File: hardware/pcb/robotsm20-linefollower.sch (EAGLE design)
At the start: 120 parts, among them IC1 BNO055, IC2 TPS43061RTER, Q1 CSD15571Q2, Q2 CSD15571Q2, Q3 CSD15571Q2, Q4 CSD15571Q2, Q5 BSS138LT3G, Q6 BSS138LT3G, Q7 BSS138LT3G, U1 STM32F405RG

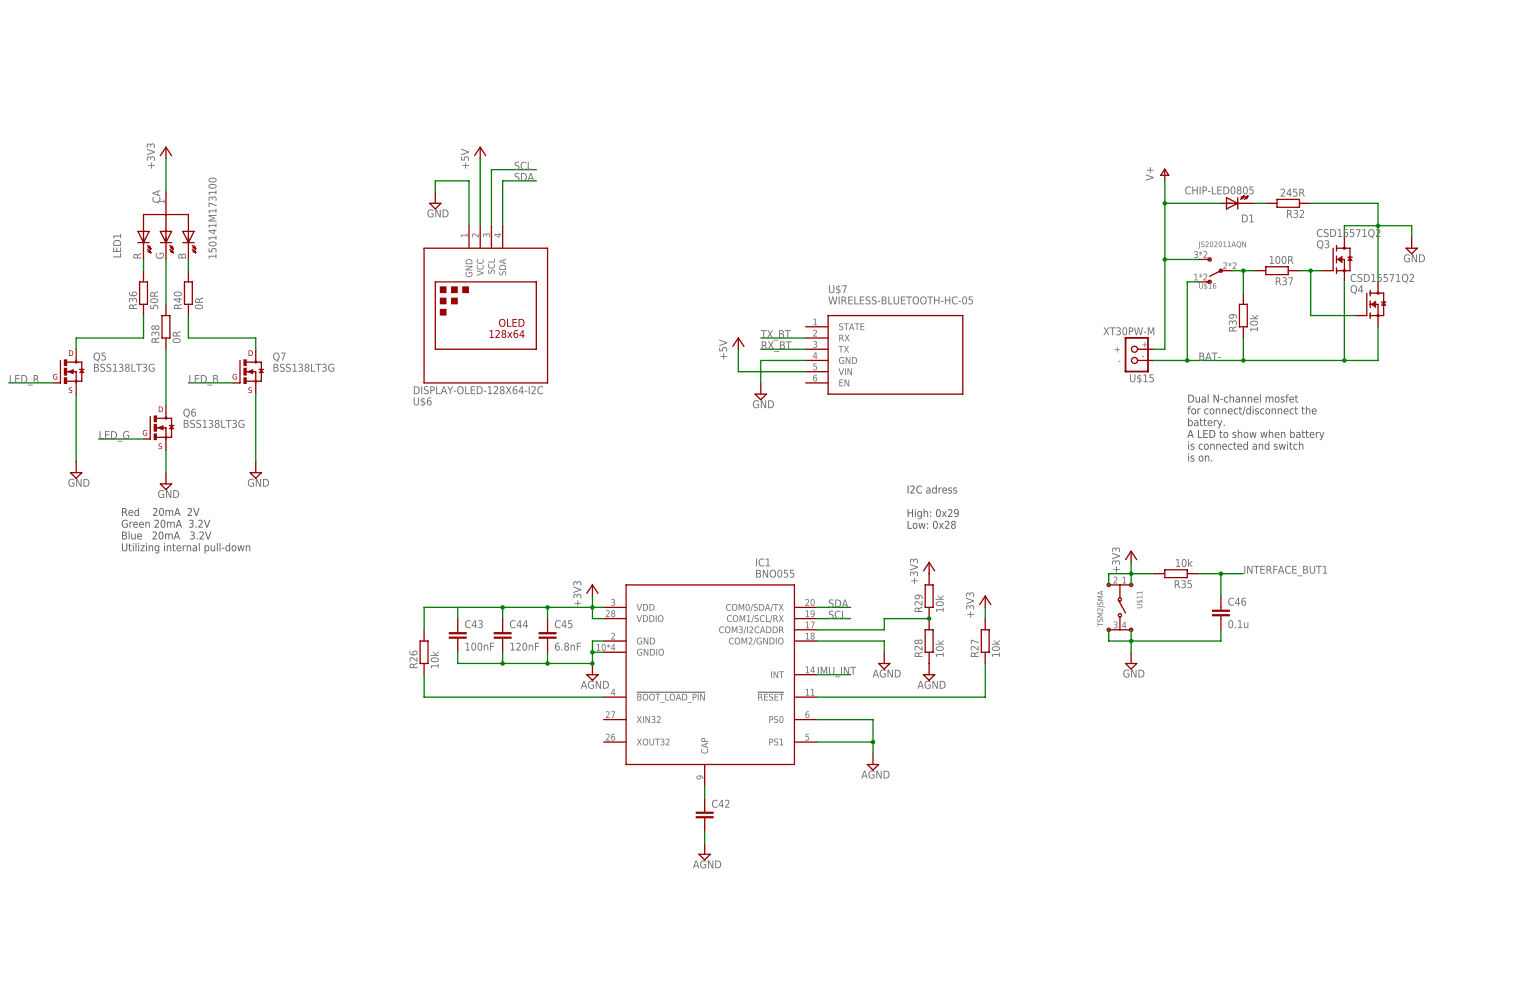
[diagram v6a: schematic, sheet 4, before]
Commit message: Added more connectors to motors and sensor
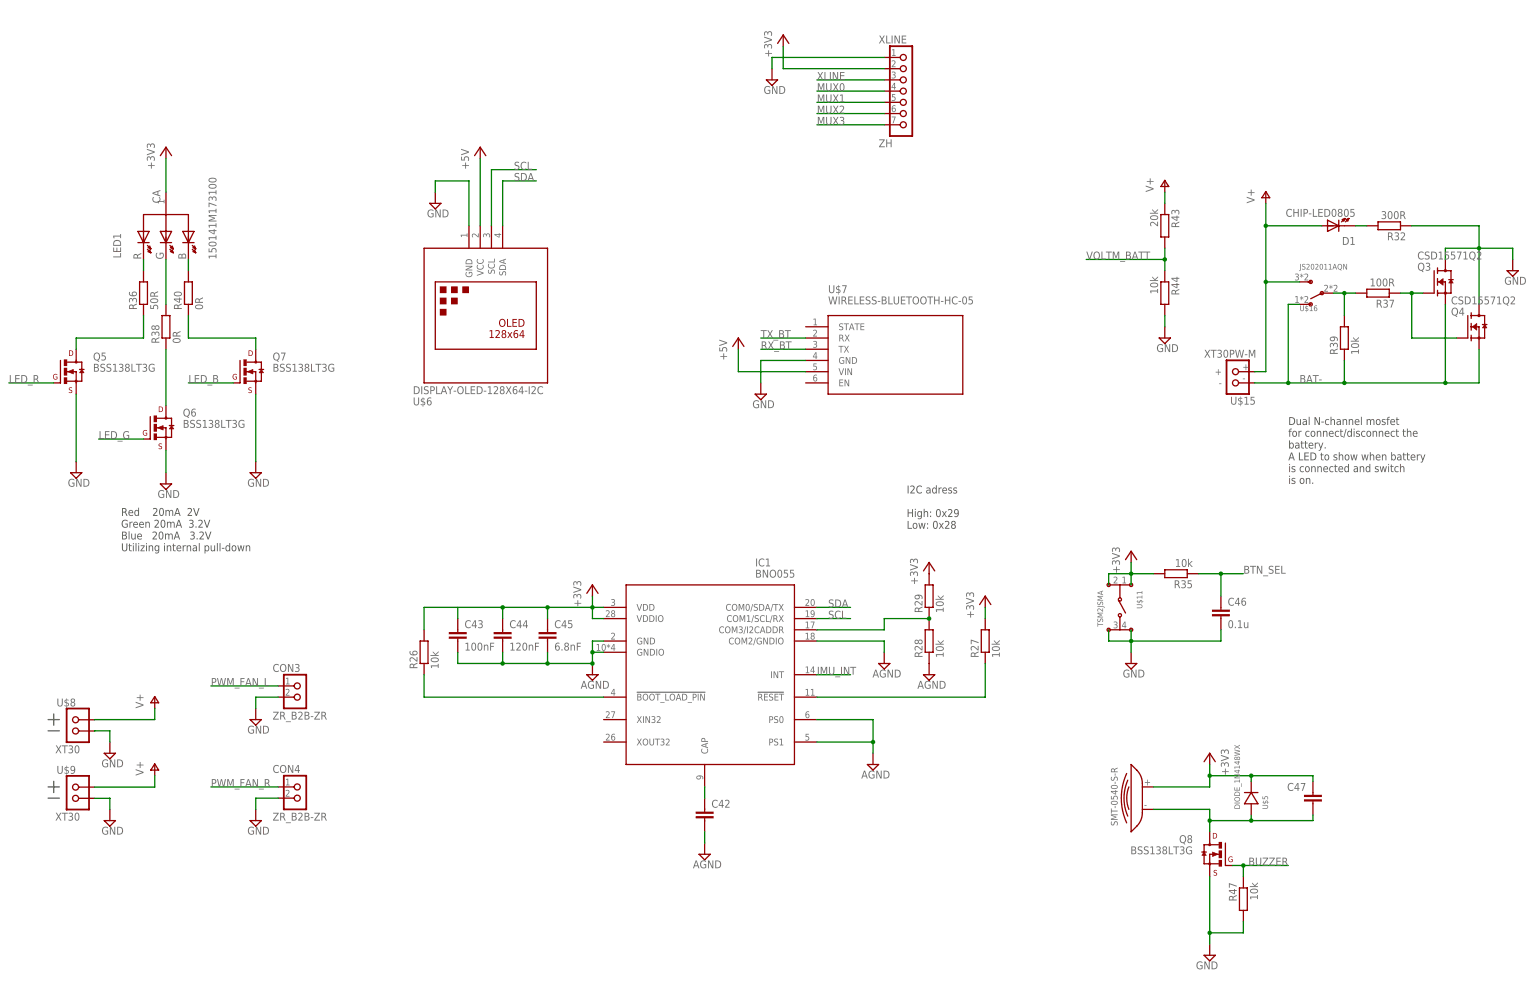
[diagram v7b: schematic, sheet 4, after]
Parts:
- added C47: (no value), rcl:C-EUC0805
- added CON3, CON4: ZR_B2B-ZR, CASE-JST:ZR_B2B-ZR
- added Q8: BSS138LT3G, CASE-Transistors:BSS138LT3G
- added R43: 20k, rcl:R-EU_R0603
- added R44, R45, R47: 10k, rcl:R-EU_R0603
- added R46: 62k, rcl:R-EU_R0603
- added U$1: SMT-0540-S-R, Isaks Bibliotek:SMT-0540-S-R
- added U$5: DIODE_1N4148WX, Isaks Bibliotek:DIODE_1N4148WX
- added U$8, U$9: XT30, CASE_DC-Connector:XT30
- added XLINE: ZH, CASE-JST:ZR_B7B-ZR
- R32: value 245R -> 300R
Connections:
- net N$66 renamed SDIO_CK
- net N$80 renamed SDIO_D0
- net VOLTM_CELL1 renamed N$25
- removed net 3.3V: BOOT.1, BOOT.2, C31.1, C32.1, C33.1, C34.1, C35.1, C37.1, C39.1, R30.1, R31.1, U1.VBAT, U1.VDDA, U1.VDD_1, U1.VDD_2, U1.VDD_3, U1.VDD_4
- removed net 3.3V1: R41.1, R42.1
- removed net CURA: C1.1, R3.2
- removed net CURB: C2.1, R4.2
- removed net GND1: PS2.GND
- removed net INTERFACE_BUT1: C46.1, R35.1
- removed net N$10: PS2.PAD, R8.1
- removed net N$25 (its old number): U1.PC0
- removed net N$35: U1.PC3
- removed net N$82: U1.PC6
- removed net N$83: U1.PC7
- removed net V+1: C14.1, PS2.EN, PS2.VIN
- new net MOTOR_L_CUR: C1.1, R3.2, U1.PC0
- new net MOTOR_R_CUR: C2.1, R4.2, U1.PC1
- new net PWM_FAN_L: CON3.1, U1.PC6
- new net PWM_FAN_R: CON4.1, U1.PC7
- new net SDIO_CMD: U1.PD2
- net +12V: now also R46.2
- net +3V3: now also BOOT.1, BOOT.2, C31.1, C32.1, C33.1, C34.1, C35.1, C37.1, C39.1, C47.1, R30.1, R31.1, R41.1, R42.1, U$1.+, U$5.-_CATHODE, U1.VBAT, U1.VDDA, U1.VDD_1, U1.VDD_2, U1.VDD_3, U1.VDD_4, XLINE.2
- net BTN_SEL: now also C46.1, R35.1, U1.PC3; no longer U1.PD2
- net BUZZER: now also Q8.G, R47.1
- net GND: now also CON3.2, CON4.2, PS2.GND, PS2.PAD, Q8.S, R44.2, R45.1, R47.2, R8.1, U$8.NEG-, U$9.NEG-, XLINE.1
- net MUX0: now also XLINE.4
- net MUX1: now also XLINE.5
- net MUX2: now also XLINE.6
- net MUX3: now also XLINE.7
- net N$33: now also C47.2, Q8.D, U$1.-, U$5.+_ANODE; no longer U1.PC1
- net V+: now also C14.1, PS2.EN, PS2.VIN, R43.1, U$8.POS+, U$9.POS+
- net VOLTM_BATT: now also R43.2, R44.1, R45.2, R46.1
- net XLINE: now also XLINE.3
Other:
- note added: "3V3 at 24V output"
- moved on the sheet: C1, C11, C12, C16, C17, C22, C23, C24, C25, C40, D1, Q3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

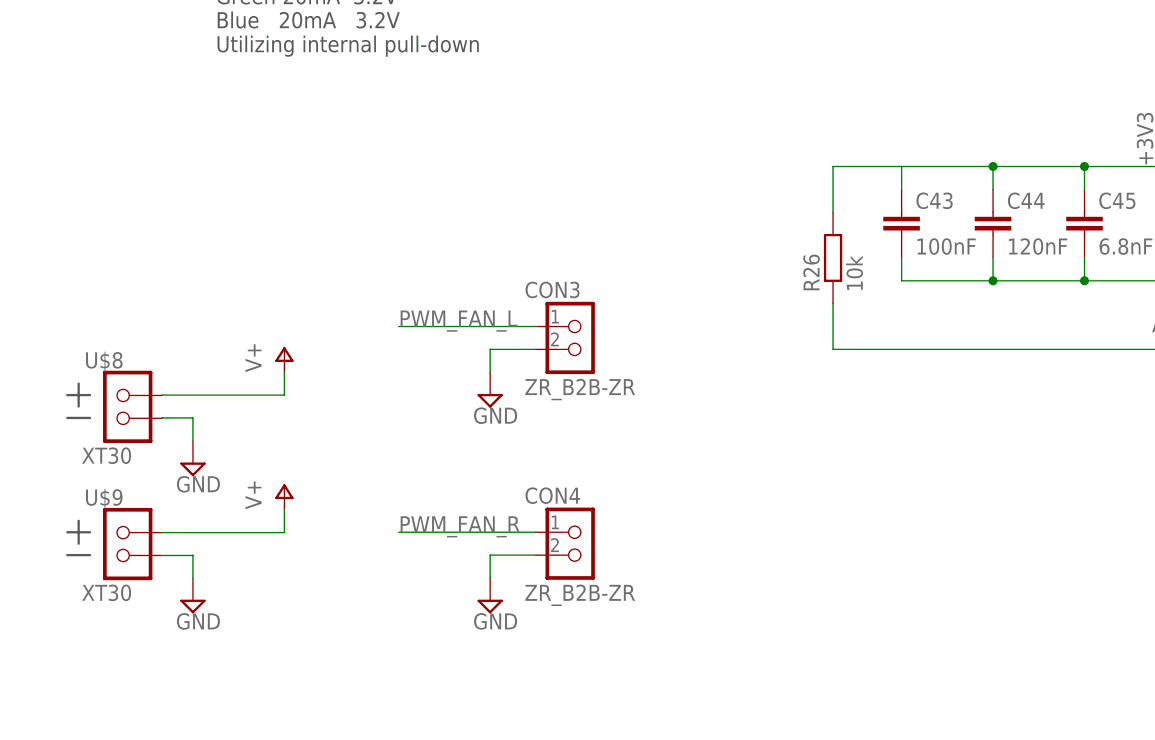
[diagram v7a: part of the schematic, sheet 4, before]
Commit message: Corrected some ERC
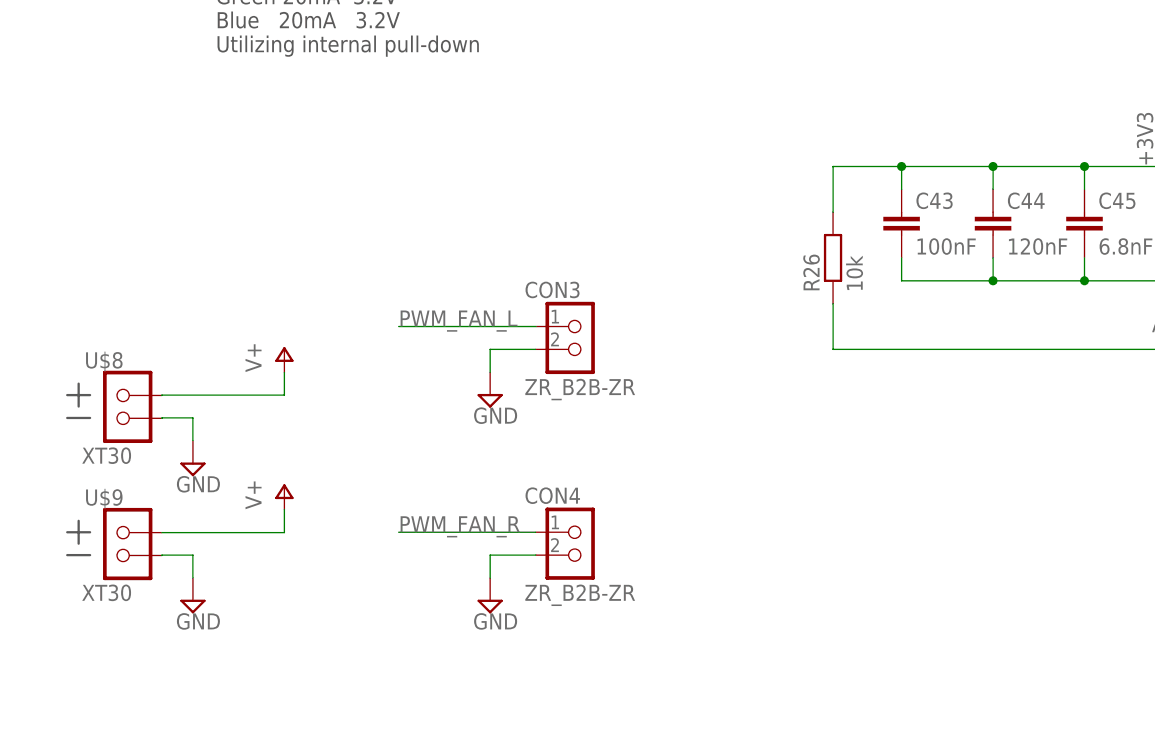
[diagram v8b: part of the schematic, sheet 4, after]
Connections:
- removed net N$2: MOTORDRIVER.VMB
- removed net N$36: C43.1
- net +3V3: now also C43.1
- net 12V: now also MOTORDRIVER.VMB
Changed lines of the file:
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@@
-</segment>
-</net>
-<net name="N$2" class="0">
-<segment>
-<pinref part="MOTORDRIVER" gate="G$1" pin="VMB"/>
-<wire x1="-35.56" y1="73.66" x2="-35.56" y2="86.36" width="0.1524" layer="91" grouprefs="MOTOR-DRIVER"/>
 </segment>
 </net>
@@
 <pinref part="MOTORDRIVER" gate="G$1" pin="VMA"/>
 <wire x1="-40.64" y1="73.66" x2="-40.64" y2="86.36" width="0.1524" layer="91" grouprefs="MOTOR-DRIVER"/>
-<wire x1="-40.64" y1="86.36" x2="-27.94" y2="86.36" width="0.1524" layer="91" grouprefs="MOTOR-DRIVER"/>
+<wire x1="-40.64" y1="86.36" x2="-35.56" y2="86.36" width="0.1524" layer="91" grouprefs="MOTOR-DRIVER"/>
 <pinref part="C7" gate="G$1" pin="1"/>
+<wire x1="-35.56" y1="86.36" x2="-27.94" y2="86.36" width="0.1524" layer="91" grouprefs="MOTOR-DRIVER"/>
 <wire x1="-27.94" y1="86.36" x2="-17.78" y2="86.36" width="0.1524" layer="91" grouprefs="MOTOR-DRIVER"/>
 <wire x1="-17.78" y1="86.36" x2="-7.62" y2="86.36" width="0.1524" layer="91" grouprefs="MOTOR-DRIVER"/>
@@
 <wire x1="0" y1="88.9" x2="0" y2="86.36" width="0.1524" layer="91" grouprefs="MOTOR-DRIVER"/>
 <junction x="0" y="86.36" grouprefs="MOTOR-DRIVER"/>
-</segment>
-</net>
-<net name="N$1" class="0">
-<segment>
-<junction x="2.54" y="-55.88" grouprefs="BIDIRECTIONAL-CURRENT-SENSOR"/>
+<pinref part="MOTORDRIVER" gate="G$1" pin="VMB"/>
+<wire x1="-35.56" y1="73.66" x2="-35.56" y2="86.36" width="0.1524" layer="91" grouprefs="MOTOR-DRIVER"/>
+<junction x="-35.56" y="86.36"/>
 </segment>
 </net>
@@
 <segment>
 <pinref part="SUPPLY81" gate="GND" pin="GND"/>
-<wire x1="-96.52" y1="-53.34" x2="-96.52" y2="-50.84" width="0.1524" layer="91" grouprefs="FAN-POWER"/>
+<wire x1="-96.52" y1="-53.34" x2="-96.52" y2="-50.8" width="0.1524" layer="91"/>
 <pinref part="U$9" gate="G$1" pin="NEG-"/>
-<wire x1="-96.52" y1="-50.8" x2="-96.52" y2="-50.84" width="0.1524" layer="91" grouprefs="FAN-POWER"/>
-<wire x1="-96.52" y1="-50.84" x2="-99.96" y2="-50.84" width="0.1524" layer="91" grouprefs="FAN-POWER"/>
+<wire x1="-96.52" y1="-50.8" x2="-99.96" y2="-50.8" width="0.1524" layer="91"/>
+<wire x1="-99.96" y1="-50.8" x2="-99.96" y2="-50.84" width="0.1524" layer="91"/>
 </segment>
 </net>
@@
 <pinref part="C44" gate="G$1" pin="1"/>
 <wire x1="2.54" y1="-7.62" x2="-7.62" y2="-7.62" width="0.1524" layer="91" grouprefs="IMU"/>
-<wire x1="-7.62" y1="-7.62" x2="-25.4" y2="-7.62" width="0.1524" layer="91" grouprefs="IMU"/>
+<wire x1="-7.62" y1="-7.62" x2="-17.78" y2="-7.62" width="0.1524" layer="91" grouprefs="IMU"/>
+<wire x1="-17.78" y1="-7.62" x2="-25.4" y2="-7.62" width="0.1524" layer="91" grouprefs="IMU"/>
 <wire x1="-7.62" y1="-10.16" x2="-7.62" y2="-7.62" width="0.1524" layer="91" grouprefs="IMU"/>
 <junction x="-7.62" y="-7.62" grouprefs="IMU"/>
@@
 <wire x1="2.54" y1="-10.16" x2="2.54" y2="-7.62" width="0.1524" layer="91" grouprefs="IMU"/>
 <junction x="2.54" y="-7.62" grouprefs="IMU"/>
+<pinref part="C43" gate="G$1" pin="1"/>
+<wire x1="-17.78" y1="-10.16" x2="-17.78" y2="-7.62" width="0.1524" layer="91" grouprefs="IMU"/>
+<junction x="-17.78" y="-7.62"/>
 </segment>
 <segment>
@@
 </segment>
 </net>
-<net name="N$36" class="0">
-<segment>
-<pinref part="C43" gate="G$1" pin="1"/>
-<wire x1="-17.78" y1="-10.16" x2="-17.78" y2="-7.62" width="0.1524" layer="91" grouprefs="IMU"/>
-</segment>
-</net>
